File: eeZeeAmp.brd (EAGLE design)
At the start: 18.8 x 13.7 mm, 19 parts, among them IC1 LM386

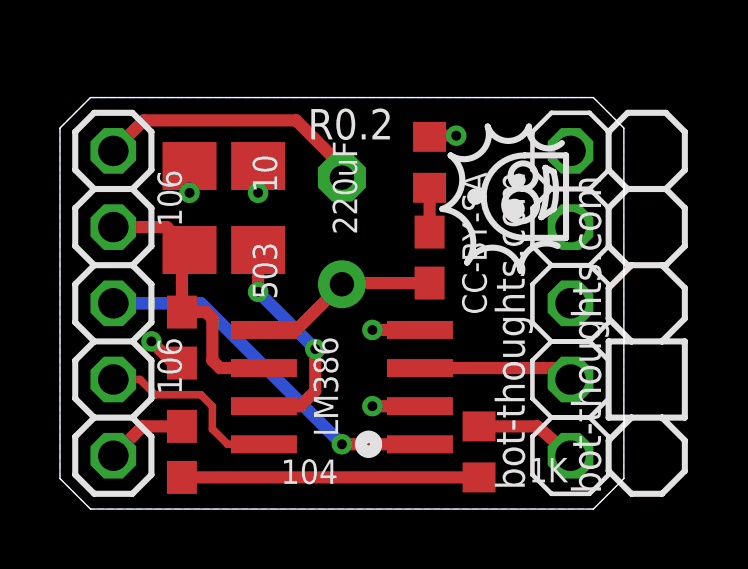
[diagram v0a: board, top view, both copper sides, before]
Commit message: Added title, OSHW logo on both sheets, relabeled gnd, audio in gnd pin header, added gain label, added cc
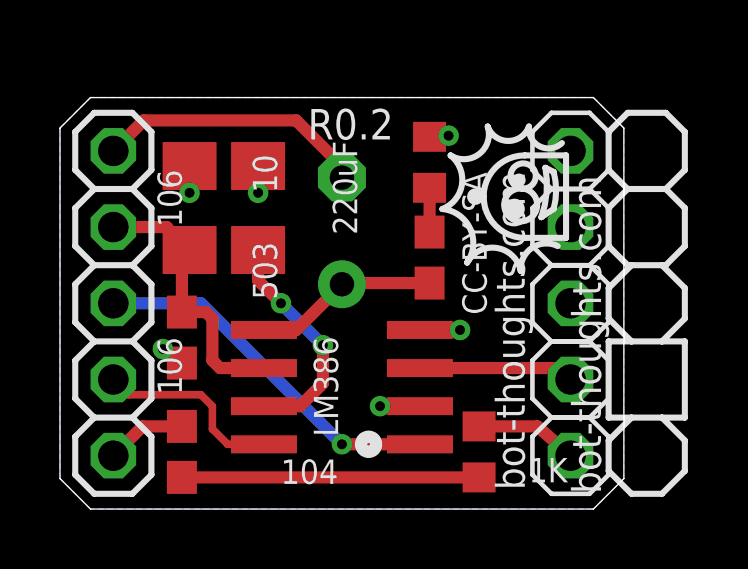
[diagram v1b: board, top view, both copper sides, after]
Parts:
- added LOGO2: OSHW-LOGOS, SparkFun-Aesthetics:OSHW-LOGO-S
- JP10: value GND -> IN-
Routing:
- net GND: track 7.17 -> 5.93 mm
